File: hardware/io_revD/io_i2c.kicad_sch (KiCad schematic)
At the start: 51 parts, among them J1 Target Interface, 2716 Pinout, J12 Conn_01x01, J13 Conn_01x01, J14 Conn_01x01, J15 Conn_01x01, J16 read region, J2 Jumper Block, J3 Jumper Block, J4 Target Interface, 2716 Pinout, J5 Conn_01x01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

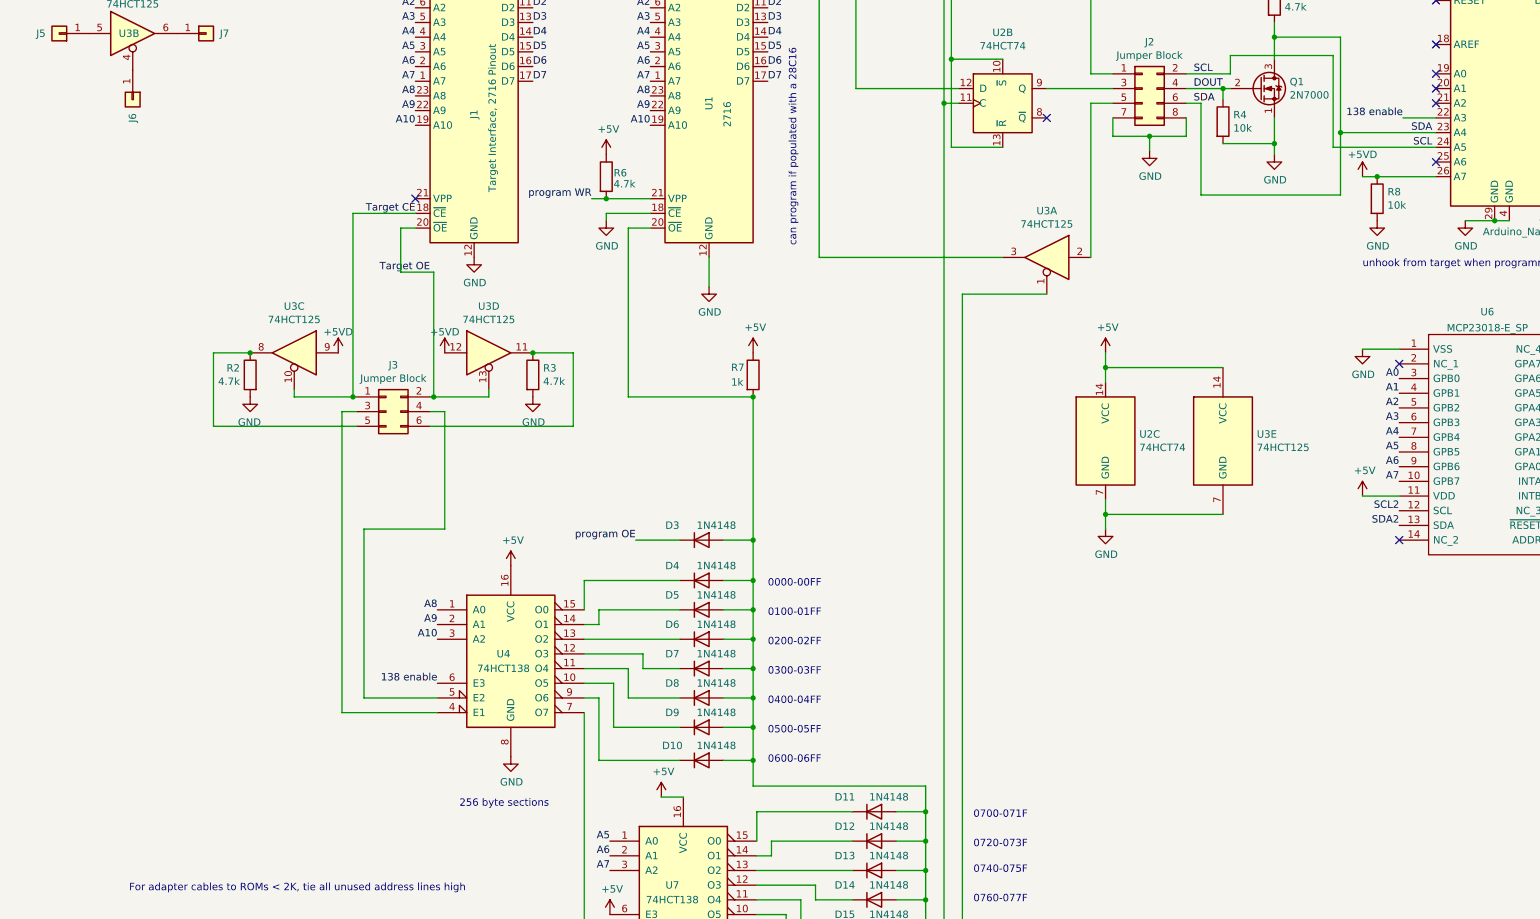
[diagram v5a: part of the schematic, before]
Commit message: update to schematic only for potential additional positive chip select
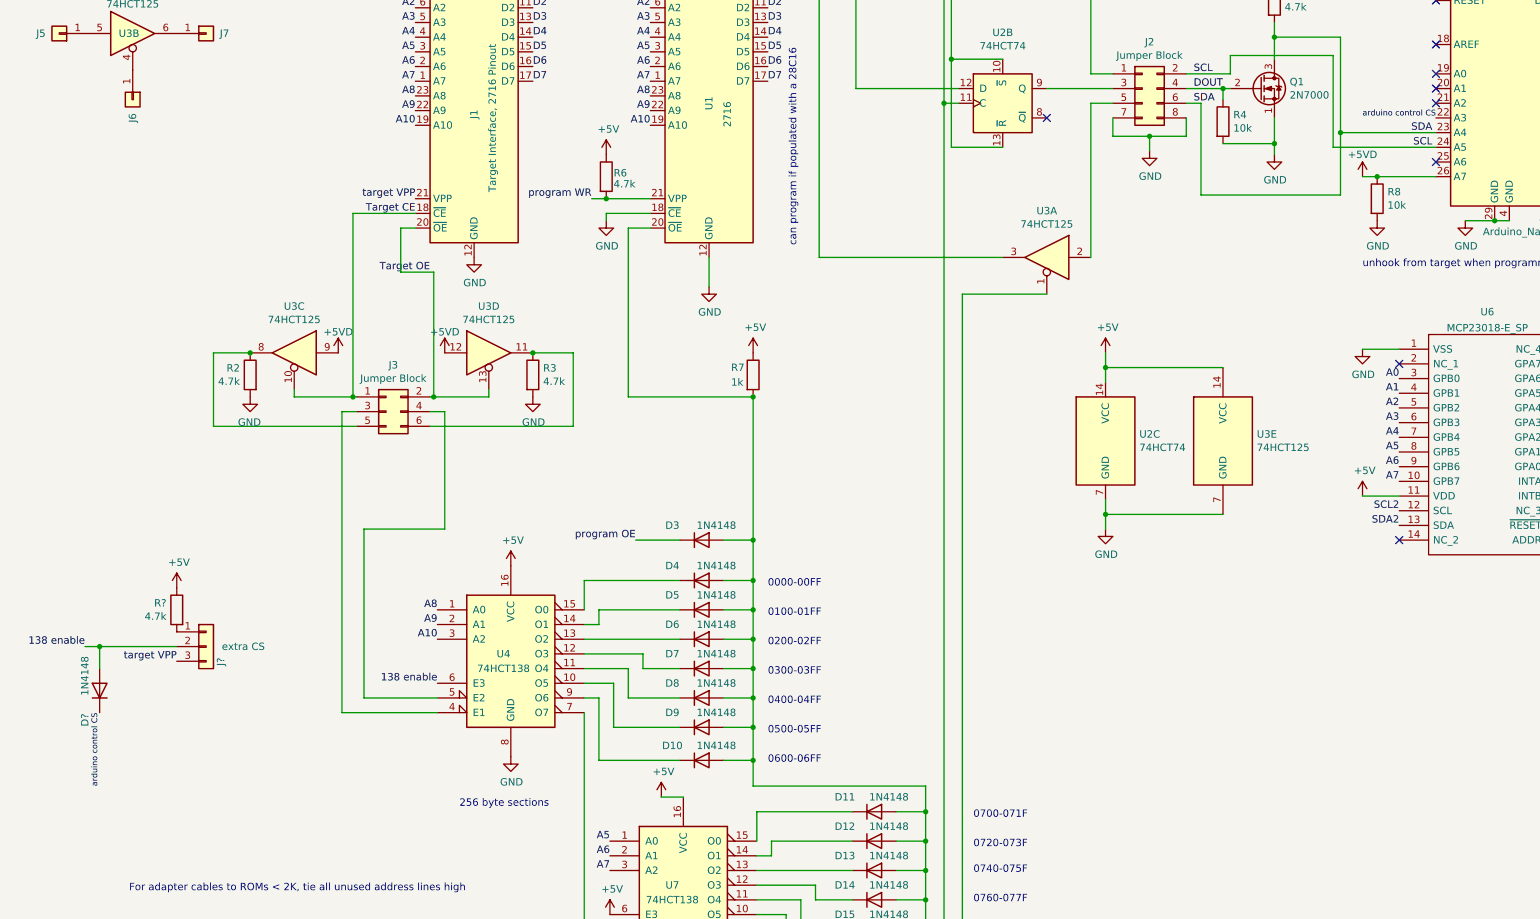
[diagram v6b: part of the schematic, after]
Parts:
- added D?: 1N4148, Diode_THT:D_DO-35_SOD27_P2.54mm_Vertical_KathodeUp, symbol Diode:1N4148
- added J?: extra CS, Connector_PinHeader_2.54mm:PinHeader_1x03_P2.54mm_Vertical, symbol Connector_Generic:Conn_01x03
- added R?: 4.7k, Resistor_THT:R_Axial_DIN0207_L6.3mm_D2.5mm_P2.54mm_Vertical, symbol Device:R
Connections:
- net +5V: now also R?.1
- net 138 enable: now also D?.2 (A), J?.2 (Pin_2); no longer A1.22 (A3)
- net target VPP: now reaches J1.21 (VPP)
- net target VPP: now also J?.3 (Pin_3)
- new net: J?.1 (Pin_1), R?.2
- new net arduino control CS: A1.22 (A3), D?.1 (K)
- no-connect marks 26 -> 25
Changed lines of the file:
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@@
   (junction (at 151.13 170.815) (diameter 0) (color 0 0 0 0)
   )
+  (junction (at 38.1 182.245) (diameter 0) (color 0 0 0 0)
+  )
   (junction (at 81.915 139.065) (diameter 0) (color 0 0 0 0)
   )
@@
   (no_connect (at 294.64 67.945))
   (no_connect (at 294.64 85.725))
-  (no_connect (at 92.71 104.775))
   (no_connect (at 294.64 100.965))
   (no_connect (at 262.89 133.35))
@@
     (stroke (width 0) (type default) (color 0 0 0 0))
   )
+  (wire (pts (xy 38.1 182.245) (xy 51.435 182.245))
+    (stroke (width 0) (type default) (color 0 0 0 0))
+  )
   (wire (pts (xy 257.81 32.385) (xy 257.81 33.655))
     (stroke (width 0) (type default) (color 0 0 0 0))
@@
     (stroke (width 0) (type default) (color 0 0 0 0))
   )
+  (wire (pts (xy 38.1 182.245) (xy 38.1 186.055))
+    (stroke (width 0) (type default) (color 0 0 0 0))
+  )
   (wire (pts (xy 212.09 133.985) (xy 232.41 133.985))
     (stroke (width 0) (type default) (color 0 0 0 0))
@@
     (stroke (width 0) (type default) (color 0 0 0 0))
   )
+  (wire (pts (xy 35.56 182.245) (xy 38.1 182.245))
+    (stroke (width 0) (type default) (color 0 0 0 0))
+  )
   (wire (pts (xy 168.91 85.725) (xy 186.69 85.725))
     (stroke (width 0) (type default) (color 0 0 0 0))
@@
     (stroke (width 0) (type default) (color 0 0 0 0))
   )
-  (wire (pts (xy 263.525 90.805) (xy 269.24 90.805))
-    (stroke (width 0) (type default) (color 0 0 0 0))
-  )
   (wire (pts (xy 274.32 108.585) (xy 279.4 108.585))
     (stroke (width 0) (type default) (color 0 0 0 0))
@@
     (effects (font (size 1.27 1.27)) (justify right bottom))
   )
+  (label "target VPP" (at 92.71 104.775 180)
+    (effects (font (size 1.27 1.27)) (justify right bottom))
+  )
   (label "A9" (at 96.52 178.435 180)
     (effects (font (size 1.27 1.27)) (justify right bottom))
@@
     (effects (font (size 1.27 1.27)) (justify left bottom))
   )
+  (label "138 enable" (at 35.56 182.245 180)
+    (effects (font (size 1.27 1.27)) (justify right bottom))
+  )
   (label "A1" (at 92.71 69.215 180)
     (effects (font (size 1.27 1.27)) (justify right bottom))
@@
     (effects (font (size 1.27 1.27)) (justify right bottom))
   )
+  (label "arduino control CS" (at 269.24 90.805 180)
+    (effects (font (size 1 1)) (justify right bottom))
+  )
   (label "A10" (at 96.52 180.975 180)
     (effects (font (size 1.27 1.27)) (justify right bottom))
@@
     (effects (font (size 1.27 1.27)) (justify right bottom))
   )
+  (label "arduino control CS" (at 38.1 193.675 270)
+    (effects (font (size 1 1)) (justify right bottom))
+  )
   (label "SDA2" (at 294.64 90.805 0)
     (effects (font (size 1.27 1.27)) (justify left bottom))
@@
     (effects (font (size 1.27 1.27)) (justify right bottom))
   )
-  (label "138 enable" (at 96.52 188.595 180)
-    (effects (font (size 1.27 1.27)) (justify right bottom))
-  )
   (label "D3" (at 132.08 59.055 0)
     (effects (font (size 1.27 1.27)) (justify left bottom))
@@
     (effects (font (size 1.27 1.27)) (justify right bottom))
   )
+  (label "target VPP" (at 51.435 184.785 180)
+    (effects (font (size 1.27 1.27)) (justify right bottom))
+  )
   (label "A7" (at 262.89 153.67 180)
     (effects (font (size 1.27 1.27)) (justify right bottom))
@@
     (effects (font (size 1.27 1.27)) (justify right bottom))
   )
+  (label "138 enable" (at 96.52 188.595 180)
+    (effects (font (size 1.27 1.27)) (justify right bottom))
+  )
   (label "D7" (at 132.08 48.895 0)
     (effects (font (size 1.27 1.27)) (justify left bottom))
@@
     (effects (font (size 1.27 1.27)) (justify right bottom))
   )
-  (label "138 enable" (at 263.525 90.805 180)
-    (effects (font (size 1.27 1.27)) (justify right bottom))
-  )
   (label "D5" (at 153.67 79.375 0)
     (effects (font (size 1.27 1.27)) (justify left bottom))
@@
     (pin "2")
   )
+  (symbol (lib_id "Connector_Generic:Conn_01x03") (at 56.515 182.245 0) (unit 1)
+    (in_bom yes) (on_board yes)
+    (property "Reference" "J?" (id 0) (at 59.055 184.15 90)
+      (effects (font (size 1.27 1.27)) (justify right))
+    )
+    (property "Value" "extra CS" (id 1) (at 66.675 182.245 0)
+      (effects (font (size 1.27 1.27)) (justify right))
+    )
+    (property "Footprint" "Connector_PinHeader_2.54mm:PinHeader_1x03_P2.54mm_Vertical" (id 2) (at 56.515 182.245 0)
+      (effects (font (size 1.27 1.27)) hide)
+    )
+    (property "Datasheet" "~" (id 3) (at 56.515 182.245 0)
+      (effects (font (size 1.27 1.27)) hide)
+    )
+    (pin "1")
+    (pin "2")
+    (pin "3")
+  )
   (symbol (lib_id "power:+5V") (at 256.54 156.21 0) (unit 1)
     (in_bom yes) (on_board yes)
@@
     (pin "1")
   )
+  (symbol (lib_id "power:+5V") (at 51.435 172.085 0) (unit 1)
+    (in_bom yes) (on_board yes)
+    (property "Reference" "#PWR?" (id 0) (at 51.435 175.895 0)
+      (effects (font (size 1.27 1.27)) hide)
+    )
+    (property "Value" "+5V" (id 1) (at 51.816 167.6908 0))
+    (property "Footprint" "" (id 2) (at 51.435 172.085 0)
+      (effects (font (size 1.27 1.27)) hide)
+    )
+    (property "Datasheet" "" (id 3) (at 51.435 172.085 0)
+      (effects (font (size 1.27 1.27)) hide)
+    )
+    (pin "1")
+  )
   (symbol (lib_id "74xx:74LS138") (at 139.065 223.52 0) (unit 1)
     (in_bom yes) (on_board yes)
@@
     (pin "1")
   )
+  (symbol (lib_id "Device:R") (at 51.435 175.895 0) (mirror y) (unit 1)
+    (in_bom yes) (on_board yes)
+    (property "Reference" "R?" (id 0) (at 49.657 174.7266 0)
+      (effects (font (size 1.27 1.27)) (justify left))
+    )
+    (property "Value" "4.7k" (id 1) (at 49.657 177.038 0)
+      (effects (font (size 1.27 1.27)) (justify left))
+    )
+    (property "Footprint" "Resistor_THT:R_Axial_DIN0207_L6.3mm_D2.5mm_P2.54mm_Vertical" (id 2) (at 53.213 175.895 90)
+      (effects (font (size 1.27 1.27)) hide)
+    )
+    (property "Datasheet" "~" (id 3) (at 51.435 175.895 0)
+      (effects (font (size 1.27 1.27)) hide)
+    )
+    (pin "1")
+    (pin "2")
+  )
+  (symbol (lib_id "Diode:1N4148") (at 38.1 189.865 90) (unit 1)
+    (in_bom yes) (on_board yes)
+    (property "Reference" "D?" (id 0) (at 35.56 194.945 0))
+    (property "Value" "1N4148" (id 1) (at 35.56 187.325 0))
+    (property "Footprint" "Diode_THT:D_DO-35_SOD27_P2.54mm_Vertical_KathodeUp" (id 2) (at 42.545 189.865 0)
+      (effects (font (size 1.27 1.27)) hide)
+    )
+    (property "Datasheet" "https://assets.nexperia.com/documents/data-sheet/1N4148_1N4448.pdf" (id 3) (at 38.1 189.865 0)
+      (effects (font (size 1.27 1.27)) hide)
+    )
+    (pin "1")
+    (pin "2")
+  )
   (symbol (lib_id "power:PWR_FLAG") (at 394.335 224.155 180) (unit 1)
     (in_bom yes) (on_board yes) (fields_autoplaced)
@@
       (reference "#PWR0138") (unit 1) (value "+5VD") (footprint "")
     )
+    (path "/67b810e7-b7f4-4fc8-89a7-9c371140114a"
+      (reference "#PWR?") (unit 1) (value "+5V") (footprint "")
+    )
     (path "/00000000-0000-0000-0000-000060a79c85"
       (reference "A1") (unit 1) (value "Arduino_Nano_v3.x") (footprint "Module:Arduino_Nano")
@@
       (reference "D18") (unit 1) (value "1N4148") (footprint "Diode_THT:D_DO-35_SOD27_P2.54mm_Vertical_KathodeUp")
     )
+    (path "/ac6b45bb-d288-4a55-b46b-b43e8c54f4b3"
+      (reference "D?") (unit 1) (value "1N4148") (footprint "Diode_THT:D_DO-35_SOD27_P2.54mm_Vertical_KathodeUp")
+    )
     (path "/00000000-0000-0000-0000-0000607e1ea2"
       (reference "J1") (unit 1) (value "Target Interface, 2716 Pinout") (footprint "Package_DIP:DIP-24_W15.24mm_Socket")
@@
       (reference "J16") (unit 1) (value "read region") (footprint "Connector_PinHeader_2.54mm:PinHeader_1x03_P2.54mm_Vertical")
     )
+    (path "/2e23db4f-942c-43a5-9246-4bbaaa1e5cf8"
+      (reference "J?") (unit 1) (value "extra CS") (footprint "Connector_PinHeader_2.54mm:PinHeader_1x03_P2.54mm_Vertical")
+    )
     (path "/00000000-0000-0000-0000-000060a18a27"
       (reference "Q1") (unit 1) (value "2N7000") (footprint "Package_TO_SOT_THT:TO-92_Wide")
@@
       (reference "R8") (unit 1) (value "10k") (footprint "Resistor_THT:R_Axial_DIN0207_L6.3mm_D2.5mm_P2.54mm_Vertical")
     )
+    (path "/9fad9287-0f1a-49d9-8c00-6b85fd067582"
+      (reference "R?") (unit 1) (value "4.7k") (footprint "Resistor_THT:R_Axial_DIN0207_L6.3mm_D2.5mm_P2.54mm_Vertical")
+    )
     (path "/00000000-0000-0000-0000-0000607df9f3"

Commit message: added layout change for extra CS mode
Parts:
- gave numbers to parts that had none: 3
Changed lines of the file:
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@@
   (symbol (lib_id "Connector_Generic:Conn_01x03") (at 56.515 182.245 0) (unit 1)
     (in_bom yes) (on_board yes)
-    (property "Reference" "J?" (id 0) (at 59.055 184.15 90)
+    (property "Reference" "J8" (id 0) (at 59.055 184.15 90)
       (effects (font (size 1.27 1.27)) (justify right))
     )
@@
   (symbol (lib_id "power:+5V") (at 51.435 172.085 0) (unit 1)
     (in_bom yes) (on_board yes)
-    (property "Reference" "#PWR?" (id 0) (at 51.435 175.895 0)
+    (property "Reference" "#PWR0139" (id 0) (at 51.435 175.895 0)
       (effects (font (size 1.27 1.27)) hide)
     )
@@
   (symbol (lib_id "Device:R") (at 51.435 175.895 0) (mirror y) (unit 1)
     (in_bom yes) (on_board yes)
-    (property "Reference" "R?" (id 0) (at 49.657 174.7266 0)
+    (property "Reference" "R9" (id 0) (at 49.657 174.7266 0)
       (effects (font (size 1.27 1.27)) (justify left))
     )
@@
   (symbol (lib_id "Diode:1N4148") (at 38.1 189.865 90) (unit 1)
     (in_bom yes) (on_board yes)
-    (property "Reference" "D?" (id 0) (at 35.56 194.945 0))
+    (property "Reference" "D19" (id 0) (at 35.56 194.945 0))
     (property "Value" "1N4148" (id 1) (at 35.56 187.325 0))
     (property "Footprint" "Diode_THT:D_DO-35_SOD27_P2.54mm_Vertical_KathodeUp" (id 2) (at 42.545 189.865 0)
@@
     )
     (path "/67b810e7-b7f4-4fc8-89a7-9c371140114a"
-      (reference "#PWR?") (unit 1) (value "+5V") (footprint "")
+      (reference "#PWR0139") (unit 1) (value "+5V") (footprint "")
     )
     (path "/00000000-0000-0000-0000-000060a79c85"
@@
     )
     (path "/ac6b45bb-d288-4a55-b46b-b43e8c54f4b3"
-      (reference "D?") (unit 1) (value "1N4148") (footprint "Diode_THT:D_DO-35_SOD27_P2.54mm_Vertical_KathodeUp")
+      (reference "D19") (unit 1) (value "1N4148") (footprint "Diode_THT:D_DO-35_SOD27_P2.54mm_Vertical_KathodeUp")
     )
     (path "/00000000-0000-0000-0000-0000607e1ea2"
@@
       (reference "J7") (unit 1) (value "Conn_01x01") (footprint "Connector_PinHeader_2.54mm:PinHeader_1x01_P2.54mm_Vertical")
     )
+    (path "/2e23db4f-942c-43a5-9246-4bbaaa1e5cf8"
+      (reference "J8") (unit 1) (value "extra CS") (footprint "Connector_PinHeader_2.54mm:PinHeader_1x03_P2.54mm_Vertical")
+    )
     (path "/19b1efdb-a9fc-4b47-8244-e1fc60c95fb0"
       (reference "J12") (unit 1) (value "Conn_01x01") (footprint "Connector_PinHeader_2.54mm:PinHeader_1x01_P2.54mm_Vertical")
@@
       (reference "J16") (unit 1) (value "read region") (footprint "Connector_PinHeader_2.54mm:PinHeader_1x03_P2.54mm_Vertical")
     )
-    (path "/2e23db4f-942c-43a5-9246-4bbaaa1e5cf8"
-      (reference "J?") (unit 1) (value "extra CS") (footprint "Connector_PinHeader_2.54mm:PinHeader_1x03_P2.54mm_Vertical")
-    )
     (path "/00000000-0000-0000-0000-000060a18a27"
       (reference "Q1") (unit 1) (value "2N7000") (footprint "Package_TO_SOT_THT:TO-92_Wide")
@@
     )
     (path "/9fad9287-0f1a-49d9-8c00-6b85fd067582"
-      (reference "R?") (unit 1) (value "4.7k") (footprint "Resistor_THT:R_Axial_DIN0207_L6.3mm_D2.5mm_P2.54mm_Vertical")
+      (reference "R9") (unit 1) (value "4.7k") (footprint "Resistor_THT:R_Axial_DIN0207_L6.3mm_D2.5mm_P2.54mm_Vertical")
     )
     (path "/00000000-0000-0000-0000-0000607df9f3"

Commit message: changed some ref des-es to make jumper numbering more sane
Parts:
- renumbered J8 to J1, J1 to J16, J16 to J5, J5 to J8
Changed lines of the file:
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@@
   (symbol (lib_id "Memory_EPROM:2716") (at 102.87 86.995 0) (unit 1)
     (in_bom yes) (on_board yes)
-    (property "Reference" "J1" (id 0) (at 102.87 90.17 90))
+    (property "Reference" "J16" (id 0) (at 102.87 90.17 90))
     (property "Value" "Target Interface, 2716 Pinout" (id 1) (at 106.045 90.805 90))
     (property "Footprint" "Package_DIP:DIP-24_W15.24mm_Socket" (id 2) (at 102.87 86.995 0)
@@
   (symbol (lib_id "Connector_Generic:Conn_01x03") (at 56.515 182.245 0) (unit 1)
     (in_bom yes) (on_board yes)
-    (property "Reference" "J8" (id 0) (at 59.055 184.15 90)
+    (property "Reference" "J1" (id 0) (at 57.785 187.325 0)
       (effects (font (size 1.27 1.27)) (justify right))
     )
@@
   (symbol (lib_id "Connector_Generic:Conn_01x03") (at 174.625 240.665 90) (unit 1)
     (in_bom yes) (on_board yes)
-    (property "Reference" "J16" (id 0) (at 176.53 238.125 90)
+    (property "Reference" "J5" (id 0) (at 176.53 238.125 90)
       (effects (font (size 1.27 1.27)) (justify right))
     )
@@
   (symbol (lib_id "Connector_Generic:Conn_01x01") (at 31.115 76.2 180) (unit 1)
     (in_bom yes) (on_board yes)
-    (property "Reference" "J5" (id 0) (at 27.94 76.2 0))
+    (property "Reference" "J8" (id 0) (at 27.94 76.2 0))
     (property "Value" "Conn_01x01" (id 1) (at 31.115 73.7386 0)
       (effects (font (size 1.27 1.27)) hide)
@@
       (reference "D19") (unit 1) (value "1N4148") (footprint "Diode_THT:D_DO-35_SOD27_P2.54mm_Vertical_KathodeUp")
     )
-    (path "/00000000-0000-0000-0000-0000607e1ea2"
-      (reference "J1") (unit 1) (value "Target Interface, 2716 Pinout") (footprint "Package_DIP:DIP-24_W15.24mm_Socket")
+    (path "/2e23db4f-942c-43a5-9246-4bbaaa1e5cf8"
+      (reference "J1") (unit 1) (value "extra CS") (footprint "Connector_PinHeader_2.54mm:PinHeader_1x03_P2.54mm_Vertical")
     )
     (path "/00000000-0000-0000-0000-000060cb41f4"
@@
       (reference "J4") (unit 1) (value "Target Interface, 2716 Pinout") (footprint "Connector_PinHeader_2.54mm:PinHeader_2x12_P2.54mm_Vertical")
     )
-    (path "/d85582d1-3609-45f5-a313-b6aab82f36d6"
-      (reference "J5") (unit 1) (value "Conn_01x01") (footprint "Connector_PinHeader_2.54mm:PinHeader_1x01_P2.54mm_Vertical")
+    (path "/4d6fcc2f-a501-4eaf-be9d-9ef118b43c3d"
+      (reference "J5") (unit 1) (value "read region") (footprint "Connector_PinHeader_2.54mm:PinHeader_1x03_P2.54mm_Vertical")
     )
     (path "/bc344a17-e2cd-4fbe-a62d-0a585f5bf2cd"
@@
       (reference "J7") (unit 1) (value "Conn_01x01") (footprint "Connector_PinHeader_2.54mm:PinHeader_1x01_P2.54mm_Vertical")
     )
-    (path "/2e23db4f-942c-43a5-9246-4bbaaa1e5cf8"
-      (reference "J8") (unit 1) (value "extra CS") (footprint "Connector_PinHeader_2.54mm:PinHeader_1x03_P2.54mm_Vertical")
+    (path "/d85582d1-3609-45f5-a313-b6aab82f36d6"
+      (reference "J8") (unit 1) (value "Conn_01x01") (footprint "Connector_PinHeader_2.54mm:PinHeader_1x01_P2.54mm_Vertical")
     )
     (path "/19b1efdb-a9fc-4b47-8244-e1fc60c95fb0"
@@
       (reference "J15") (unit 1) (value "Conn_01x01") (footprint "Connector_PinHeader_2.54mm:PinHeader_1x01_P2.54mm_Vertical")
     )
-    (path "/4d6fcc2f-a501-4eaf-be9d-9ef118b43c3d"
-      (reference "J16") (unit 1) (value "read region") (footprint "Connector_PinHeader_2.54mm:PinHeader_1x03_P2.54mm_Vertical")
+    (path "/00000000-0000-0000-0000-0000607e1ea2"
+      (reference "J16") (unit 1) (value "Target Interface, 2716 Pinout") (footprint "Package_DIP:DIP-24_W15.24mm_Socket")
     )
     (path "/00000000-0000-0000-0000-000060a18a27"
